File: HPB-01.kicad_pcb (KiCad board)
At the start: 2 copper layers, 60 x 27 mm, 55 parts, among them J1 USB_A, J4 USB_C_Receptacle_USB2.0, J5 Pad, J6 Pad, J7 Battery Pad, J8 Battery Pad, Q1 RU207C, Q4 RU20P7C, Q5 IRF7832, Q6 IRF7832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

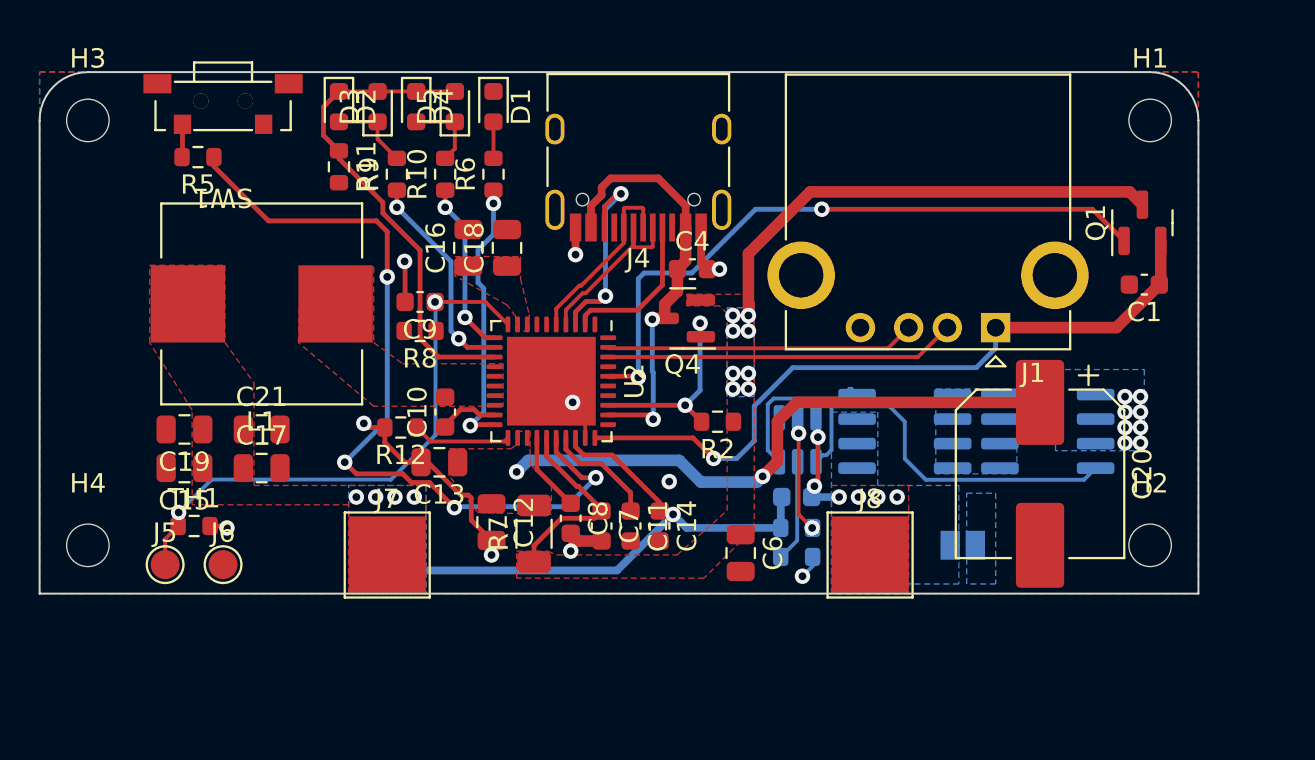
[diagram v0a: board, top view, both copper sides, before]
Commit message: ERC and DRC correction
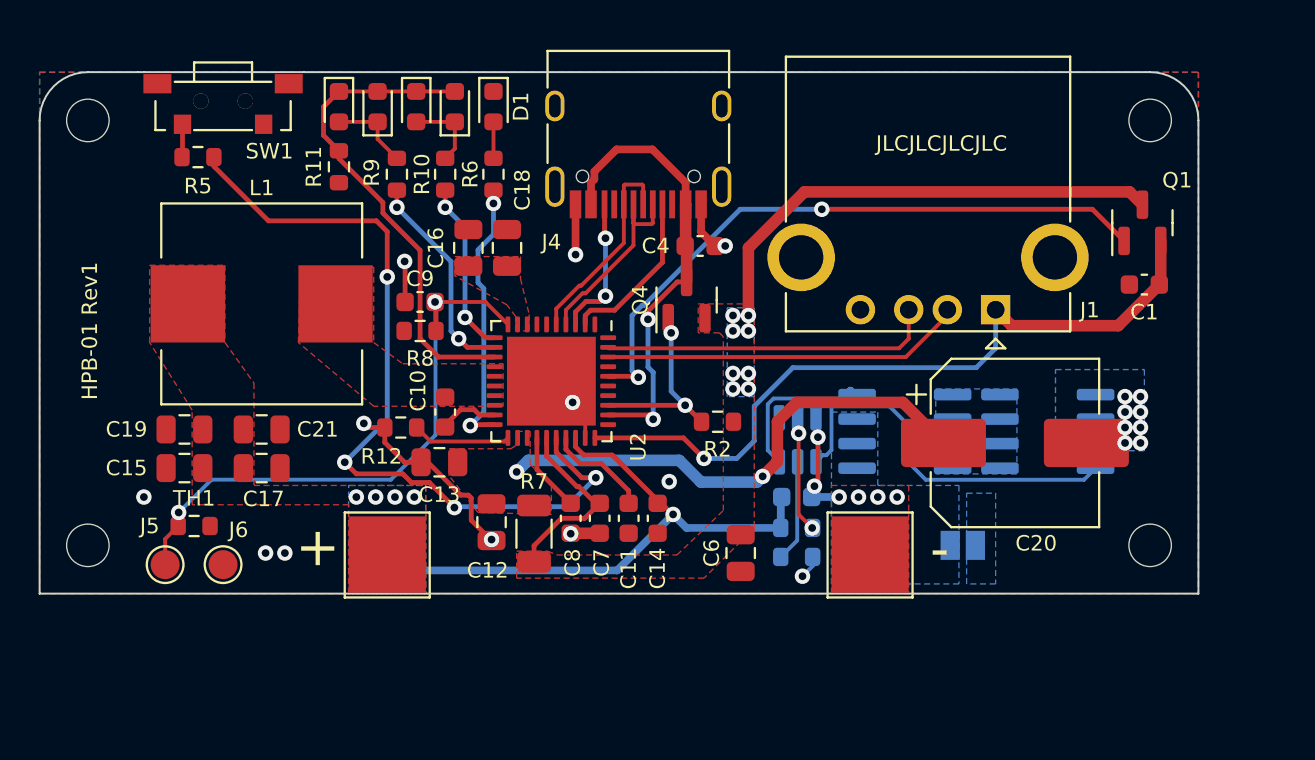
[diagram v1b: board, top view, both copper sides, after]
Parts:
- moved C20 2.06 mm to (150.5, 89.2), turned to 0 degrees
- moved C4 1.26 mm to (134.2, 79.0)
- moved J4 1.20 mm to (131.0, 72.8)
- moved Q4 0.97 mm to (133.5, 81.8), turned to 90 degrees
- moved J1 0.93 mm to (149.5, 82.3)
- moved C11 0.41 mm to (130.5, 93.1)
- moved C14 0.41 mm to (132.0, 93.1)
- moved C7 0.41 mm to (129.0, 93.1)
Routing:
- net /VSP: track 34.8 -> 30.7 mm
- net /CC2: track 10.4 -> 7.31 mm
- net /VBUS: track 22.0 -> 23.6 mm
- net GND: track 26.0 -> 24.4 mm, vias 18 -> 20
- net /NTC: track 29.1 -> 30.6 mm
- net /USBA1_P: track 16.0 -> 17.3 mm
- net /VIN: track 37.4 -> 38.6 mm
- net /USBC_P: track 9.52 -> 10.7 mm
- net /USBC_N: track 9.55 -> 10.7 mm
- net /VOUT1G: track 34.0 -> 33.3 mm
- net /USBA1_N: track 18.2 -> 18.8 mm
- net /CC1: track 8.09 -> 8.61 mm
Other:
- outline, holes or cut-outs redrawn
- board text added: "+"
- board text added: "-"
- board text added: "HPB-01 Rev1"
- board text added: "JLCJLCJLCJLC"

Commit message: Change the layout (bigger)
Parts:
- removed C1, C4: 10uF, Capacitor_SMD:C_0603_1608Metric
- removed C10, C5, C7, C8, C9: 100nF, Capacitor_SMD:C_0603_1608Metric
- removed C11, C14: 2.2uF, Capacitor_SMD:C_0603_1608Metric
- removed C12, C13, C15, C16, C17, C18, C19, C21, C6: 22uF, Capacitor_SMD:C_0805_2012Metric
- removed C20: 220uF, Capacitor_SMD:CP_Elec_8x10.5
- removed D1: GREEN, LED_SMD:LED_0603_1608Metric
- removed D2, D3, D4, D5: BLUE, LED_SMD:LED_0603_1608Metric
- removed J1: USB_A, Connector_USB:USB_A_CONNFLY_DS1095-WNR0
- removed J4: USB_C_Receptacle_USB2.0, Connector_USB:USB_C_Receptacle_HRO_TYPE-C-31-M-12
- removed J5, J6: Pad, TestPoint:TestPoint_Pad_D1.5mm
- removed J7, J8: Battery Pad, TestPoint:TestPoint_Pad_4.0x4.0mm
- removed JP1: SolderJumper_2_Open, Jumper:SolderJumper-2_P1.3mm_Open_Pad1.0x1.5mm
- removed L1: 2.2uH, Inductor_SMD:L_Wuerth_HCI-1050
- removed Q1: RU207C, Package_TO_SOT_SMD:SOT-23
- removed Q4: RU20P7C, Package_TO_SOT_SMD:SOT-23
- removed Q5, Q6: IRF7832, Package_SO:SOIC-8_3.9x4.9mm_P1.27mm
- removed R10, R6, R9: 100, Resistor_SMD:R_0603_1608Metric
- removed R11: NC, Resistor_SMD:R_0603_1608Metric
- removed R12: 114k, Resistor_SMD:R_0603_1608Metric
- removed R2: 10k, Resistor_SMD:R_0603_1608Metric
- removed R3: 2k, Resistor_SMD:R_0603_1608Metric
- removed R4: 470, Resistor_SMD:R_0603_1608Metric
- removed R5: 1k, Resistor_SMD:R_0603_1608Metric
- removed R7: 0.01, Resistor_SMD:R_1206_3216Metric
- removed R8: 82k(1%), Resistor_SMD:R_0603_1608Metric
- removed SW1: SW_Push, huconn-footprint:tact_switch 1TS002G-1300-3500-CT
- removed TH1: 100k@25C 4250K, Resistor_SMD:R_0603_1608Metric
- removed U1: S-8261ABJMD-G3JT2S, Package_TO_SOT_SMD:SOT-23-6
- removed U2: IP5328P, Package_DFN_QFN:QFN-40-1EP_6x6mm_P0.5mm_EP4.6x4.6mm
- moved H2 6.80 mm to (161.5, 100.0)
- moved H4 5.50 mm to (102.5, 100.0)
- moved H1 4.00 mm to (161.5, 72.5)
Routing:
- net /KEY: track 41.6 -> 0.00 mm, vias 4 -> 0
- net /VIN: track 38.6 -> 0.00 mm, vias 1 -> 0
- net /VMID: track 35.2 -> 0.00 mm, vias 8 -> 0
- net /VOUT1G: track 33.3 -> 0.00 mm, vias 2 -> 0
- net /VSP: track 30.7 -> 0.00 mm, vias 2 -> 0
- net /NTC: track 30.6 -> 0.00 mm, vias 2 -> 0
- net /VBAT: track 29.7 -> 0.00 mm, vias 5 -> 0
- net /L3: track 25.5 -> 0.00 mm
- net GND: track 24.4 -> 0.00 mm, vias 20 -> 0
- net /VBUS: track 23.6 -> 0.00 mm, vias 2 -> 0
- net /DFET: track 19.9 -> 0.00 mm
- net /USBA1_N: track 18.8 -> 0.00 mm
- net /USBA1_P: track 17.3 -> 0.00 mm
- net /LIGHT: track 14.2 -> 0.00 mm, vias 2 -> 0
- net /L2: track 11.1 -> 0.00 mm, vias 2 -> 0
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- removed copper zone on B.Cu, net /VBAT
- removed copper zone on B.Cu, net /VBAT-
- removed copper zone on B.Cu, net /VMID
- removed copper zone on F.Cu, net /VMID
- removed copper zone on F.Cu, net /VSP
- removed copper zone on F.Cu, net Net-(C10-Pad2)
- removed copper zone on B.Cu, net Net-(Q5-Pad5)
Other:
- board size 60 x 27 mm -> 64 x 32.5 mm
- board text removed: "HPB-01 Rev1"
- board text removed: "JLCJLCJLCJLC"

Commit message: [WIP] positioning parts on new layout (90%)
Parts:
- added C1: 10uF, Capacitor_SMD:C_0603_1608Metric, F.Cu at (146.5, 87.0)
- added C10: 100nF, Capacitor_SMD:C_0603_1608Metric, F.Cu at (129.0, 92.7)
- added C11: 2.2uF, Capacitor_SMD:C_0603_1608Metric, F.Cu at (127.8, 83.6)
- added C12: 22uF, Capacitor_SMD:C_0805_2012Metric, F.Cu at (120.6, 97.2)
- added C13: 22uF, Capacitor_SMD:C_0805_2012Metric, F.Cu at (133.4, 88.6)
- added C14: 2.2uF, Capacitor_SMD:C_0603_1608Metric, F.Cu at (126.7, 82.5)
- added C15: 22uF, Capacitor_SMD:C_0805_2012Metric, F.Cu at (153.0, 96.0)
- added C16: 22uF, Capacitor_SMD:C_0805_2012Metric, F.Cu at (118.6, 97.2)
- added C17: 22uF, Capacitor_SMD:C_0805_2012Metric, F.Cu at (151.0, 96.0)
- added C18: 22uF, Capacitor_SMD:C_0805_2012Metric, F.Cu at (114.6, 97.2)
- added C19: 22uF, Capacitor_SMD:C_0805_2012Metric, F.Cu at (149.0, 96.0)
- added C20: 22uF, Capacitor_SMD:C_0805_2012Metric, F.Cu at (132.0, 90.0)
- added C21: 22uF, Capacitor_SMD:C_0805_2012Metric, F.Cu at (147.0, 96.0)
- added C22: 22uF, Capacitor_SMD:C_0805_2012Metric, F.Cu at (134.8, 87.2)
- added C23: 22uF, Capacitor_SMD:C_0805_2012Metric, F.Cu at (136.2, 85.8)
- added C24: 22uF, Capacitor_SMD:C_0805_2012Metric, F.Cu at (116.6, 97.2)
- added C4: 10uF, Capacitor_SMD:C_0603_1608Metric, F.Cu at (115.0, 82.5)
- added C5: 100nF, Capacitor_SMD:C_0603_1608Metric, F.Cu at (108.7, 90.5)
- added C6: 22uF, Capacitor_SMD:C_0805_2012Metric, F.Cu at (129.5, 76.5)
- added C7: 100nF, Capacitor_SMD:C_0603_1608Metric, F.Cu at (128.9, 84.7)
- added C8: 100nF, Capacitor_SMD:C_0603_1608Metric, F.Cu at (130.0, 85.8)
- added C9: 100nF, Capacitor_SMD:C_0603_1608Metric, F.Cu at (124.3, 97.4)
- added D1: GREEN, LED_SMD:LED_0603_1608Metric, F.Cu at (161.4, 96.4)
- added D2: BLUE, LED_SMD:LED_0603_1608Metric, F.Cu at (161.4, 85.2)
- added D3: BLUE, LED_SMD:LED_0603_1608Metric, F.Cu at (161.4, 88.0)
- added D4: BLUE, LED_SMD:LED_0603_1608Metric, F.Cu at (161.4, 90.8)
- added D5: BLUE, LED_SMD:LED_0603_1608Metric, F.Cu at (161.4, 93.6)
- added J1: USB_A, HUCONN-Connector_USB:USB_A_FEMALE_905-662A203S10200, F.Cu at (147.0, 74.5)
- added J4: USB_C_Receptacle_USB2.0, Connector_USB:USB_C_Receptacle_HRO_TYPE-C-31-M-12, F.Cu at (118.5, 73.9)
- added J5: Pad, TestPoint:TestPoint_Pad_D1.5mm, F.Cu at (129.0, 101.0)
- added J6: Pad, TestPoint:TestPoint_Pad_D1.5mm, F.Cu at (125.3, 100.9)
- added JP1: SolderJumper_2_Open, Jumper:SolderJumper-2_P1.3mm_Open_Pad1.0x1.5mm, F.Cu at (103.7, 95.1)
- added L1: 2.2uH, Inductor_SMD:L_Wuerth_HCI-1050, F.Cu at (139.2, 97.0)
- added Q1: RU207C, Package_TO_SOT_SMD:SOT-23, F.Cu at (143.6, 85.4)
- added Q4: RU20P7C, Package_TO_SOT_SMD:SOT-23, F.Cu at (117.5, 82.5)
- added Q5: IRF7832, Package_SO:SOIC-8_3.9x4.9mm_P1.27mm, F.Cu at (107.6, 79.5)
- added Q6: IRF7832, Package_SO:SOIC-8_3.9x4.9mm_P1.27mm, F.Cu at (107.4, 85.8)
- added R10: 100, Resistor_SMD:R_0603_1608Metric, F.Cu at (157.0, 95.0)
- added R11: NC, Resistor_SMD:R_0603_1608Metric, F.Cu at (157.0, 91.8)
- added R12: 110k, Resistor_SMD:R_0603_1608Metric, F.Cu at (130.9, 91.4)
- added R2: 10k, Resistor_SMD:R_0603_1608Metric, F.Cu at (117.6, 85.2)
- added R3: 2k, Resistor_SMD:R_0603_1608Metric, F.Cu at (104.4, 90.6)
- added R4: 470, Resistor_SMD:R_0603_1608Metric, F.Cu at (109.3, 93.6)
- added R5: 1k, Resistor_SMD:R_0603_1608Metric, F.Cu at (157.4, 83.2)
- added R6: 100, Resistor_SMD:R_0603_1608Metric, F.Cu at (157.0, 93.4)
- added R7: 0.01, Resistor_SMD:R_1206_3216Metric, F.Cu at (132.0, 84.0)
- added R8: 82k(1%), Resistor_SMD:R_0603_1608Metric, F.Cu at (125.9, 97.4)
- added R9: 100, Resistor_SMD:R_0603_1608Metric, F.Cu at (157.0, 90.2)
- added SW1: SW_Push, Button_Switch_SMD:SW_Push_1P1T-MP_NO_Horizontal_Alps_SKRTLAE010, F.Cu at (162.5, 79.0)
- added TH1: 100k@25C 4250K, Resistor_SMD:R_0603_1608Metric, F.Cu at (127.5, 97.4)
- added U1: S-8261ABJMD-G3JT2S, Package_TO_SOT_SMD:SOT-23-6, F.Cu at (108.8, 97.9)
- added U2: IP5328P, Package_DFN_QFN:QFN-40-1EP_6x6mm_P0.5mm_EP4.6x4.6mm, F.Cu at (123.0, 90.1)
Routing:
- net /VBAT: track 0.00 -> 4.90 mm
- net /VSYS: track 0.00 -> 4.76 mm
- net /VMID: track 0.00 -> 4.56 mm
- net /VREG: track 0.00 -> 4.47 mm
- net /KEY: track 0.00 -> 2.87 mm, vias 0 -> 1
- added copper zone on B.Cu, net /VBAT
- added copper zone on B.Cu, net /VBAT-
- removed copper zone on F.Cu, net /VBAT
- removed copper zone on F.Cu, net /VBAT-
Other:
- outline, holes or cut-outs redrawn
- copper layers 2 -> 4

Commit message: PCB artwork complete
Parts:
- J5, J6, JP1: moved to B.Cu
- moved JP1 9.44 mm to (112.2, 99.2)
- moved C5 8.42 mm to (107.3, 98.8)
- moved Q5 6.72 mm to (105.0, 85.7), turned to 90 degrees
- moved R4 5.39 mm to (104.1, 95.0), turned to -90 degrees
- moved Q6 3.10 mm to (110.5, 85.7), turned to 90 degrees
- moved J5 3.00 mm to (132.0, 101.1), turned to 180 degrees
- moved U1 2.91 mm to (106.9, 95.7), turned to -90 degrees
- moved C18 2.81 mm to (114.4, 94.4), turned to -135 degrees
- moved R3 2.80 mm to (106.9, 91.8), turned to -90 degrees
- moved C12 2.43 mm to (118.6, 98.6), turned to -135 degrees
- moved J6 2.41 mm to (127.7, 101.1), turned to 180 degrees
- moved R11 1.95 mm to (157.0, 89.8)
- moved R10 1.65 mm to (157.0, 93.3)
- moved R9 1.60 mm to (157.0, 91.8)
- moved C24 1.59 mm to (115.8, 95.8), turned to -135 degrees
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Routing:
- net /VBAT: track 4.90 -> 78.9 mm, vias 0 -> 10
- net /L3: track 0.00 -> 55.6 mm, vias 0 -> 4
- net /LIGHT: track 0.00 -> 36.7 mm, vias 0 -> 2
- net /L2: track 0.00 -> 35.8 mm, vias 0 -> 2
- net /L1: track 0.00 -> 35.8 mm, vias 0 -> 2
- net /USBA1_N: track 0.00 -> 35.2 mm, vias 0 -> 2
- net /USBA1_P: track 0.00 -> 35.1 mm, vias 0 -> 2
- net /KEY: track 2.87 -> 36.9 mm, vias 1 -> 2
- net /VOUT1G: track 0.00 -> 26.9 mm, vias 0 -> 2
- net /VSYS: track 4.76 -> 31.5 mm, vias 0 -> 2
- net /VIN: track 0.00 -> 25.3 mm, vias 0 -> 2
- net /USBC_P: track 0.00 -> 23.9 mm, vias 0 -> 2
- net /USBC_N: track 0.00 -> 22.4 mm, vias 0 -> 2
- net /CC2: track 0.00 -> 21.8 mm, vias 0 -> 2
- net /VBUS: track 0.00 -> 20.8 mm, vias 0 -> 2
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- added copper zone on F.Cu, net /VBAT
- added copper zone on F.Cu, net /VBAT-
- added copper zone on F.Cu, net /VIN
- added copper zone on F.Cu, net /VMID
- added copper zone on F.Cu, net /VSYS
- added copper zone on F.Cu, net Net-(C10-Pad2)
- added copper zone on F.Cu, net Net-(Q5-Pad5)
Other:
- board text added: "JLCJLCJLCJLC"

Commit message: WIP: bug fix and make some improvement
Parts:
- added C2: 10uF, Capacitor_SMD:C_0603_1608Metric, F.Cu at (112.4, 72.2)
- added C25: 10uF, Capacitor_SMD:C_1206_3216Metric, F.Cu at (149.4, 95.4)
- added C3: 10uF, Capacitor_SMD:C_1206_3216Metric, F.Cu at (147.0, 100.1)
- added R1: 10k, Resistor_SMD:R_0603_1608Metric, F.Cu at (123.2, 82.8)
- C11, C14: value 2.2uF -> 2.2uF/0603/16V
- C15, C17, C19, C21: value 22uF -> 10uF; footprint Capacitor_SMD:C_0805_2012Metric -> Capacitor_SMD:C_1206_3216Metric
- C4: value 10uF -> 10uF/25V
- R12: value 110k -> 100k/0402/50V; footprint Resistor_SMD:R_0603_1608Metric -> Resistor_SMD:R_0402_1005Metric
- moved C21 4.84 mm to (151.8, 95.4)
- moved C17 4.40 mm to (149.4, 100.1), turned to -90 degrees
- moved C15 4.27 mm to (151.8, 100.1), turned to -90 degrees
- moved C19 2.09 mm to (147.0, 95.4)
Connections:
- net /VBAT renamed /VBAT+
- C1 pad 1: /VIN -> /VOUT1
- J1 pad 1: /VIN -> /VOUT1
- Q1 pad 2: /VIN -> /VOUT1
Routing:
- net /VIN: track 25.3 -> 0.00 mm, vias 2 -> 0
- net /VOUT1: track 0.00 -> 25.0 mm, vias 0 -> 2
- net /VBUSG: track 7.69 -> 4.02 mm
- net GND: track 18.2 -> 19.8 mm, vias 30 -> 32
- net /VSYS: track 31.5 -> 32.6 mm
- net /VREG: vias 0 -> 1
- added copper zone on F.Cu, net /VOUT1
- added copper zone on In1.Cu, net GND
- added copper zone on In2.Cu, net GND
- removed copper zone on F.Cu, net /VIN

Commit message: revision 1.1
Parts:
- removed C18, C24: 22uF, Capacitor_SMD:C_0805_2012Metric
- C15, C17, C19, C21, C25, C3: value 10uF -> 22uF; footprint Capacitor_SMD:C_1206_3216Metric -> Capacitor_SMD:C_0805_2012Metric
- moved C2 14.4 mm to (117.9, 85.5), turned to 180 degrees
- moved C16 13.3 mm to (124.9, 86.4), turned to 180 degrees
- moved J5 12.3 mm to (121.9, 94.0)
- moved C15 12.3 mm to (141.0, 94.2), turned to 90 degrees
- moved C12 12.0 mm to (124.9, 88.4), turned to 180 degrees
- moved J6 11.6 mm to (118.5, 94.0)
- moved C7 11.5 mm to (140.4, 84.5), turned to 0 degrees
- moved C14 10.6 mm to (137.3, 82.1), turned to 0 degrees
- moved C8 10.4 mm to (140.4, 86.0), turned to 0 degrees
- moved R7 10.1 mm to (141.3, 87.9), turned to 180 degrees
- moved U2 10.0 mm to (131.5, 84.8), turned to 0 degrees
- moved C22 9.97 mm to (144.1, 90.8), turned to -90 degrees
- moved C11 9.50 mm to (137.3, 83.6), turned to 0 degrees
- moved R8 9.26 mm to (120.1, 89.4), turned to 180 degrees
- moved C13 8.69 mm to (124.9, 90.4), turned to 180 degrees
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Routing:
- net /VSYS: track 32.6 -> 7.61 mm, vias 2 -> 10
- net /VOUT2: track 0.00 -> 18.4 mm, vias 0 -> 2
- net /VREG: track 4.47 -> 22.5 mm, vias 1 -> 2
- net /VBAT+: track 78.9 -> 63.2 mm, vias 10 -> 50
- net /USBA1_P: track 35.3 -> 23.1 mm
- net /LIGHT: track 36.7 -> 24.9 mm
- net /USBA1_N: track 35.5 -> 23.8 mm
- net /VBUSG: track 4.02 -> 13.1 mm
- net /KEY: track 36.9 -> 29.1 mm
- net /VBUS: track 20.8 -> 28.4 mm
- net /L3: track 55.6 -> 48.9 mm
- net /L2: track 35.8 -> 31.5 mm
- net /USBC_N: track 22.4 -> 26.5 mm, vias 2 -> 3
- net /VOUT1G: track 26.4 -> 22.7 mm
- net /L1: track 35.8 -> 32.2 mm
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- added copper zone on F.Cu, net /VBUS
- added copper zone on B.Cu, net /VMID
- added copper zone on In1.Cu, net /VMID
- added copper zone on In2.Cu, net /VMID
- added copper zone on B.Cu, net /VSYS
- removed copper zone on F.Cu, net /VOUT1
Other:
- outline, holes or cut-outs redrawn
- board text removed: "JLCJLCJLCJLC"
